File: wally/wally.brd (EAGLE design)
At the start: 41 x 101 mm, 102 parts, among them IC1 ESP32-S3-WROOM-1U-N16, IC2 XTLV61048DBVR, IC3 TLV1117LV33DCYR, IC4 DPS310XTSA1, IC6 LSM6DSV16BXTR, IC7 MLX90395KLW-BBA-001-SP, J1 MSD-4-A, J2 QWIIC_RIGHT_ANGLE, J3 QWIIC_RIGHT_ANGLE, J5 USB4105-GF-A, U1 RA-01H

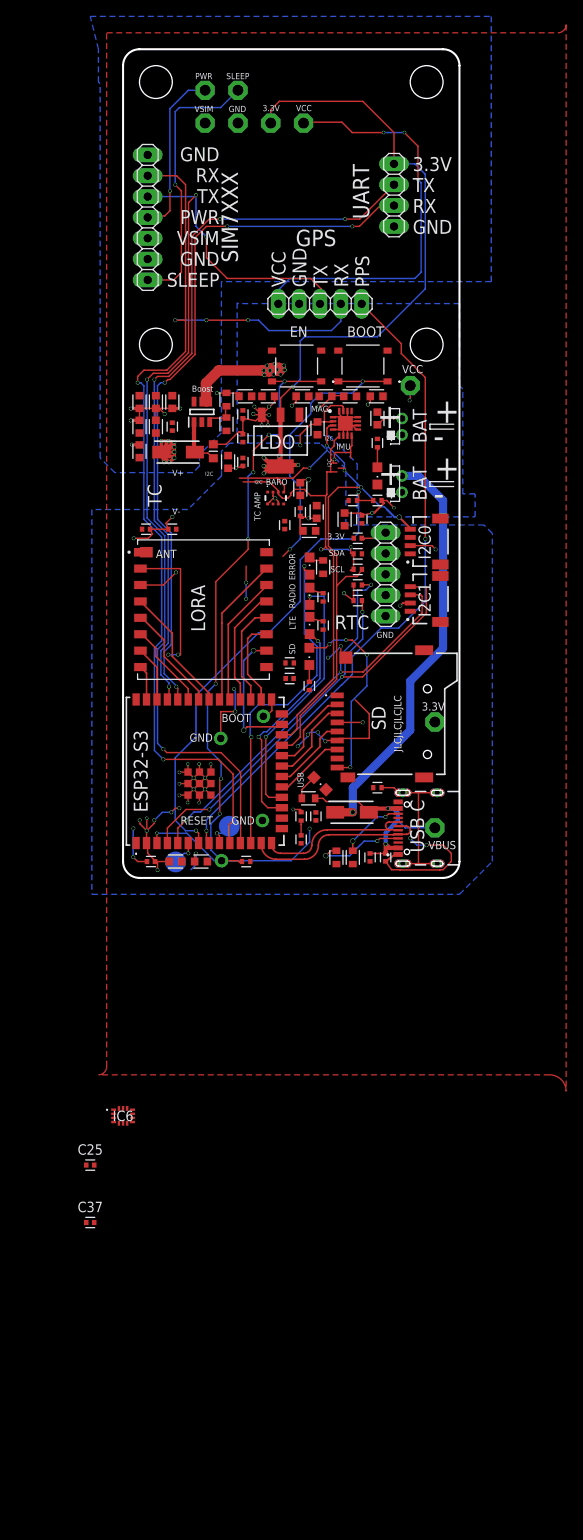
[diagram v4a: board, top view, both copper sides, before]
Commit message: rewire qwiic connectors
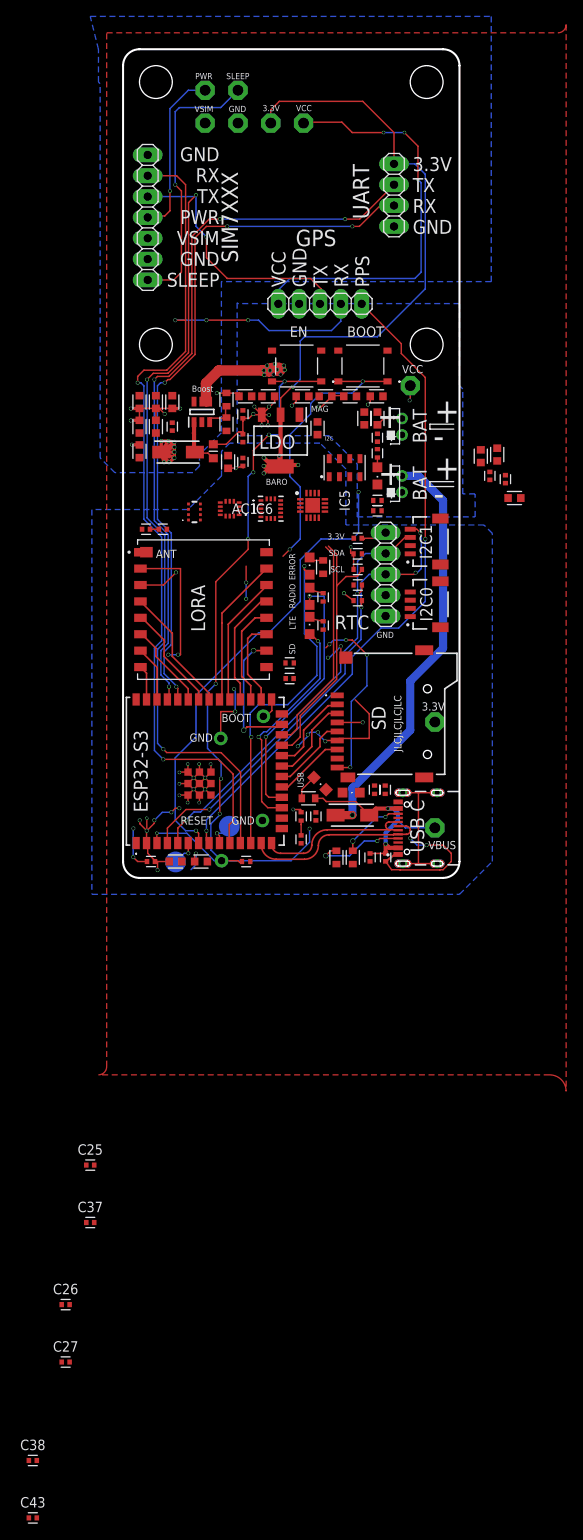
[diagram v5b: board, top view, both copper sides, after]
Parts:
- added AC1: H3LIS331DLTR, SamacSys_Parts:LIS3DHTR
- added C26, C27, C38, C43: 100n, Capacitor:CAPC1005X60
- added IC5: MS560702BA03-50, SamacSys_Parts:MS5607-02BA03
- moved IC6 75.1 mm to (13.0, -56.0), turned to 180 degrees
- moved C28 25.7 mm to (44.7, -52.0)
- moved C42 25.3 mm to (47.7, -54.7)
- moved C29 25.3 mm to (46.6, -52.4)
- moved C41 23.1 mm to (45.6, -49.4)
- moved C40 22.4 mm to (43.6, -49.6)
- moved LED1 17.4 mm to (27.8, -90.6), turned to 270 degrees
- moved R15 14.9 mm to (30.6, -90.2), turned to 90 degrees
- moved C7 12.5 mm to (29.4, -45.0), turned to 270 degrees
- moved IC7 10.8 mm to (23.1, -55.6)
- moved C1 10.1 mm to (31.0, -47.4), turned to 90 degrees
- moved IC4 10.0 mm to (8.70, -56.4), turned to 270 degrees
- moved J2 7.65 mm to (35.0, -67.7)
- moved J3 7.00 mm to (35.0, -60.0)
- moved R10 3.25 mm to (31.0, -56.2), turned to 0 degrees
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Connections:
- removed net N$5: IC6.14
- removed net N$6: IC6.13
- net 3V3: now also AC1.1, AC1.14, AC1.15, AC1.8, C26.1, C27.1, C38.1, C43.1, IC5.1, IC5.2
- net GND: now also AC1.10, AC1.12, AC1.13, AC1.16, AC1.5, AC1.7, C26.2, C27.2, C38.2, C43.2, IC5.3, IC5.4, IC5.5, IC5.6
- net SCL0: now also AC1.4, IC5.8, IC6.13
- net SDA0: now also AC1.6, IC5.7, IC6.14
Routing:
- net SCL0: track 76.5 -> 32.5 mm, vias 5 -> 0
- net 3V3: track 165.4 -> 127.4 mm, vias 29 -> 20
- net SDA0: track 58.6 -> 26.6 mm, vias 1 -> 0
- net GND: track 108.9 -> 95.3 mm
- net VCC: track 162.1 -> 153.2 mm, vias 26 -> 24
- net SDA1: track 59.9 -> 53.3 mm, vias 3 -> 2
- net VSENSE: track 60.1 -> 56.9 mm
- net SHLD: track 19.8 -> 17.5 mm
- net N$1: track 2.04 -> 0.00 mm
- net N$49: track 24.3 -> 22.3 mm
- net SCL1: track 59.8 -> 58.2 mm, vias 3 -> 4
- net N$9: track 2.49 -> 1.19 mm
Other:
- board text removed: "IMU"
- board text removed: "TC AMP"

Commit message: route new i2c traces
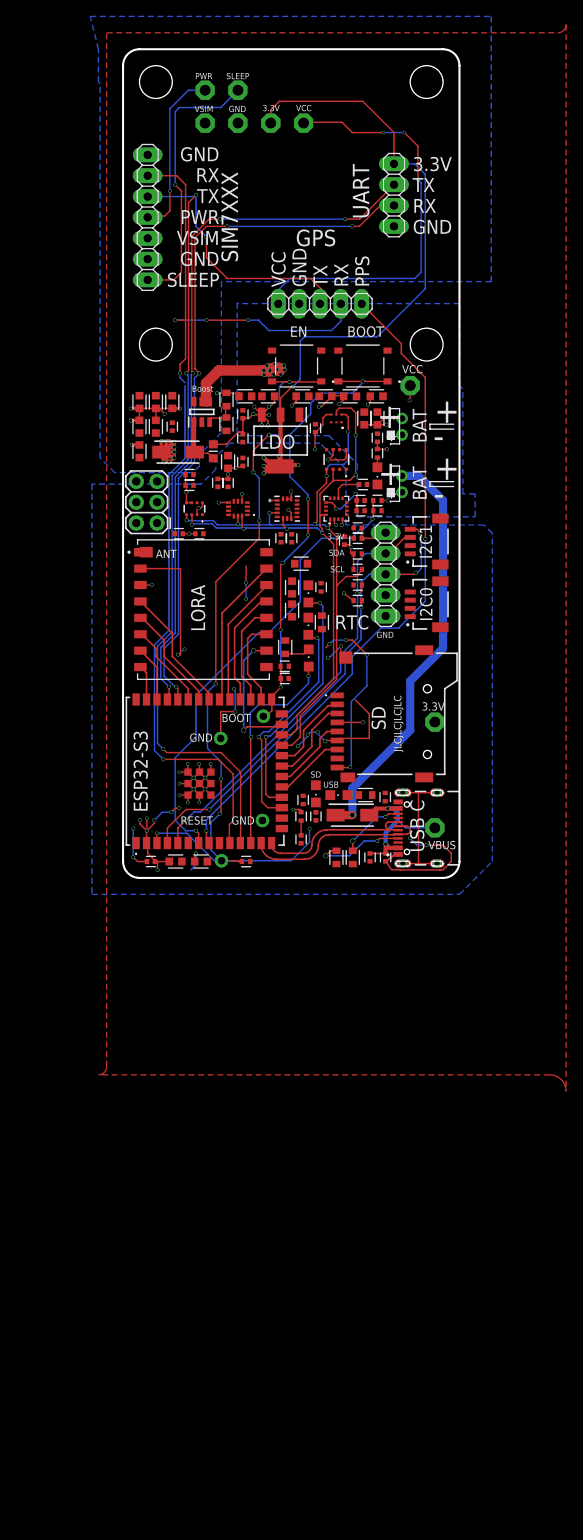
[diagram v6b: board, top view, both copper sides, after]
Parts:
- removed IC5: MS560702BA03-50, SamacSys_Parts:MS5607-02BA03
- removed TP14, TP15: PTR1B2,54, testpad:B2,54
- added C44, C46: 1u, Capacitor:CAPC1005X60
- added C45: 100n, Capacitor:CAPC1005X60
- added IC8: APDS-9253-001, SamacSys_Parts:APDS9253001
- added IC9: BME688, SamacSys_Parts:BME688
- added J6: FEMALE 2x3, SparkFun-Connectors:2X3
- C24: value 470n -> 10u; device Capacitor:CAPC1608X85 -> Capacitor:CAPC1005X60
- IC4: value DPS310XTSA1 -> DPS368XTSA1; device SamacSys_Parts:DPS310XTSA1 -> SamacSys_Parts:DPS368XTSA1
- IC7: value MLX90395KLW-BBA-001-SP -> MMC5983MA; device SamacSys_Parts:QFN50P300X300X100-17N -> SamacSys_Parts:MMC5983MA
- LED5: value LEDG -> LEDY
- R19: value 33 -> 75; device Resistor:RESC1005X40 -> Resistor:RESC1608X60
- R5, R6, R7, R8: value 10k -> 5k1
- moved C43 129.1 mm to (28.9, -56.2)
- moved C38 123.6 mm to (28.9, -55.0)
- moved C27 104.1 mm to (20.6, -59.6), turned to 270 degrees
- moved C26 97.0 mm to (19.2, -59.6), turned to 270 degrees
- moved C37 91.7 mm to (12.8, -52.9), turned to 270 degrees
- moved C25 84.6 mm to (11.6, -52.9), turned to 270 degrees
- moved C29 38.5 mm to (8.10, -53.1), turned to 0 degrees
- moved C28 36.6 mm to (8.10, -51.9), turned to 0 degrees
- moved C41 31.4 mm to (20.6, -68.4)
- moved C40 28.0 mm to (20.6, -65.6)
- moved C42 27.2 mm to (21.7, -62.7)
- moved LED6 11.2 mm to (22.6, -74.2)
- moved R20 10.8 mm to (19.8, -72.9), turned to 90 degrees
- moved C24 8.82 mm to (29.2, -53.0), turned to 0 degrees
- moved R15 8.79 mm to (21.9, -91.5)
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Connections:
- removed net ERR_LED: IC1.12, LED6.A
- removed net LTE_STATUS: IC1.17, LED4.A
- removed net RAD_STATUS: IC1.18, LED5.A
- new net A2: IC1.18, J6.6, LED4.A
- new net A3: IC1.6, J6.3
- new net A4: IC1.9, J6.5
- new net N$6: C24.1, IC7.10
- net 3V3: now also C44.1, C45.1, C46.1, IC4.5, IC7.13, IC7.4, IC8.4, IC9.2, IC9.6, IC9.8; no longer C24.2, IC5.1, IC5.2, IC7.15, IC7.8
- net A0: now also IC1.12, J6.2, LED6.A; no longer IC1.6, TP15.TP
- net A1: now also IC1.17, J6.4, LED5.A; no longer IC1.9, TP14.TP
- net GND: now also C24.2, C44.2, C45.2, C46.2, IC8.1, IC9.1, IC9.5, IC9.7, J6.1; no longer C24.1, IC5.3, IC5.4, IC5.5, IC5.6, IC7.1, IC7.10, IC7.12, IC7.13, IC7.14, IC7.16, IC7.17, IC7.4, IC7.6, IC7.7
- net SCL0: now also IC7.1, IC8.6, IC9.4; no longer IC5.8, IC7.3
- net SDA0: now also IC7.16, IC8.5, IC9.3; no longer IC5.7, IC7.5
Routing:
- net SDA0: track 26.6 -> 72.6 mm, vias 0 -> 6
- net SCL0: track 32.5 -> 75.0 mm, vias 0 -> 7
- net ERR_LED: track 41.2 -> 0.00 mm, vias 2 -> 0
- net RAD_STATUS: track 32.0 -> 0.00 mm, vias 2 -> 0
- net 3V3: track 127.4 -> 158.4 mm, vias 20 -> 36
- net A2: track 0.00 -> 30.1 mm, vias 0 -> 2
- net LTE_STATUS: track 27.3 -> 0.00 mm, vias 2 -> 0
- net A1: track 3.18 -> 27.6 mm, vias 1 -> 2
- net A0: track 3.24 -> 26.6 mm, vias 1 -> 2
- net BOOT: track 37.3 -> 58.8 mm, vias 2 -> 6
- net VBUS: track 26.8 -> 19.4 mm
- net VCC: track 153.2 -> 159.9 mm, vias 24 -> 28
- net RX1: track 123.9 -> 119.7 mm
- net N$6: track 0.00 -> 3.90 mm
- net N$4: track 3.15 -> 0.00 mm
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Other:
- board text removed: "BARO"
- board text removed: "ERROR"
- board text removed: "I2C"
- board text removed: "LTE"
- board text removed: "MAG"
- board text removed: "RADIO"

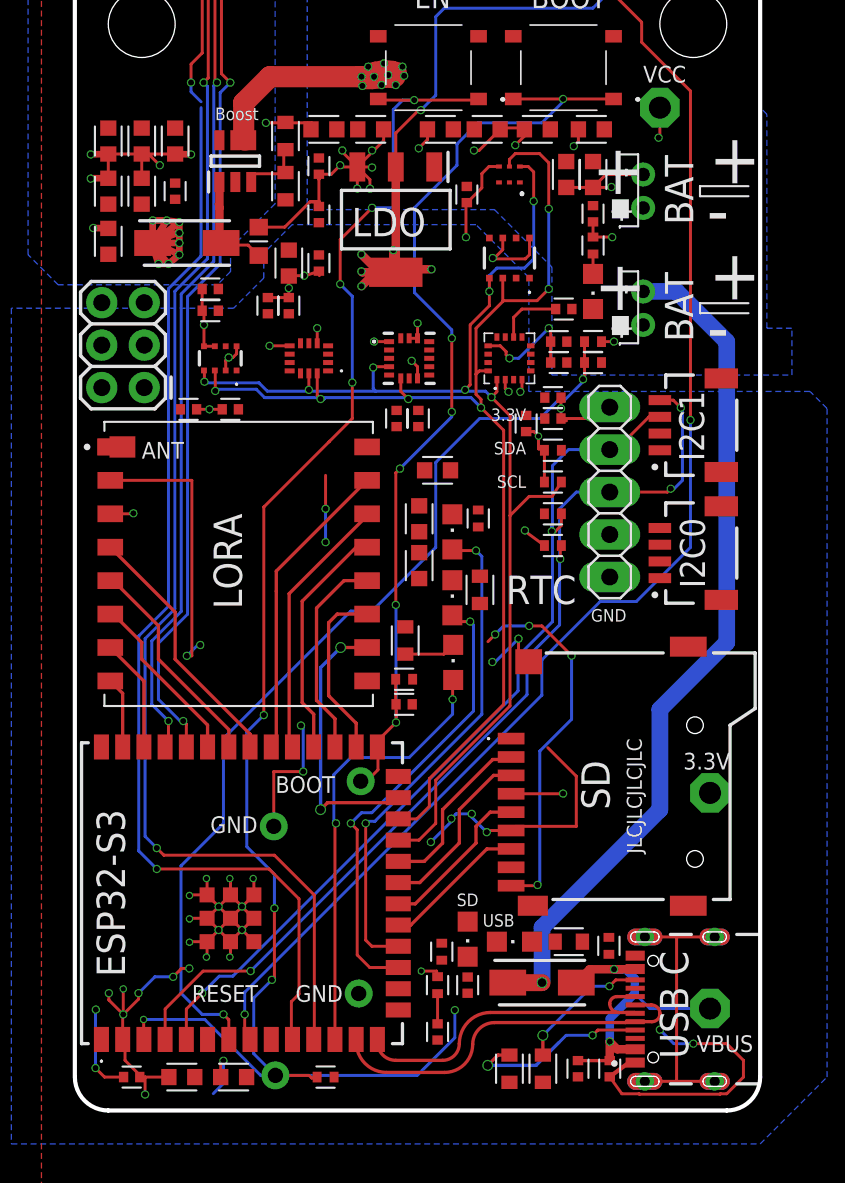
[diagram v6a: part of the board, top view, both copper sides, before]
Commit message: complete routing
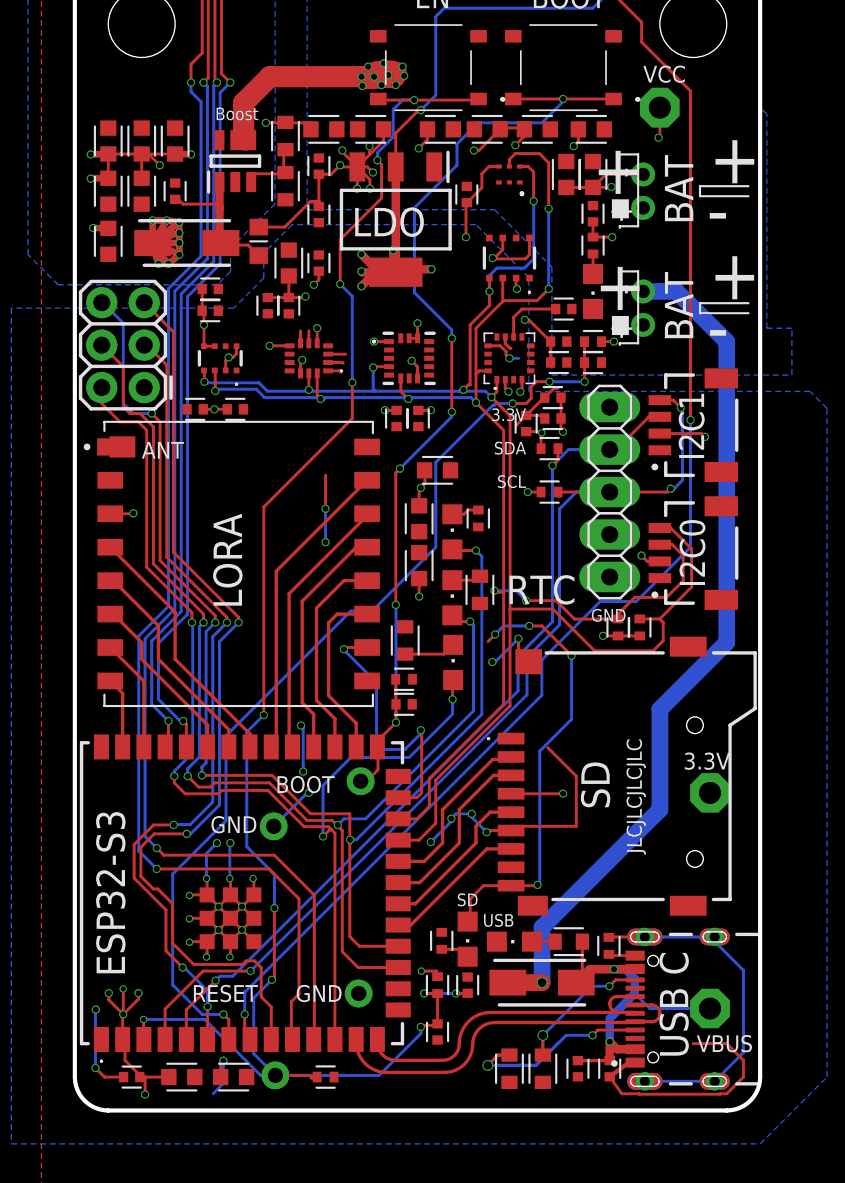
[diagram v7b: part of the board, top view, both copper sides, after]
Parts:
- moved R5 11.3 mm to (32.5, -72.1), turned to 90 degrees
- moved R6 10.1 mm to (33.8, -72.1), turned to 90 degrees
- moved R7 3.91 mm to (28.4, -61.4)
- moved R8 3.21 mm to (28.4, -64.0)
- moved R15 0.65 mm to (21.9, -90.8)
- moved C23 0.40 mm to (7.20, -59.0)
- moved C19 0.30 mm to (9.60, -59.0)
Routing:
- net A4: track 0.00 -> 55.9 mm, vias 0 -> 2
- net A3: track 0.00 -> 49.1 mm, vias 0 -> 4
- net A2: track 30.1 -> 75.0 mm, vias 2 -> 5
- net A1: track 27.6 -> 68.7 mm, vias 2 -> 4
- net A0: track 26.6 -> 65.8 mm, vias 2 -> 4
- net SCL0: track 75.0 -> 91.8 mm
- net SDA0: track 72.6 -> 89.1 mm, vias 6 -> 8
- net GND: track 95.0 -> 89.7 mm, vias 28 -> 27
- net N$49: track 22.3 -> 26.5 mm
- net SHLD: track 17.5 -> 21.2 mm
- net VBUS: track 19.4 -> 22.0 mm
- net N$2: track 6.89 -> 9.44 mm
- net SCL1: track 58.2 -> 60.5 mm, vias 4 -> 3
- net 3V3: track 158.4 -> 160.5 mm, vias 36 -> 43
- net N$8: track 0.51 -> 2.26 mm
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
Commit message: export new wally
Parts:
- J6: device SparkFun-Connectors:2X3 -> SparkFun-Connectors:2X3-NS
- moved J6 2.91 mm to (2.85, -55.1)
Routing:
- net GND: track 89.7 -> 115.9 mm, vias 27 -> 40
- net N$49: track 26.5 -> 4.19 mm, vias 4 -> 0
- net 3V3: track 160.5 -> 181.1 mm, vias 43 -> 45
- net A3: track 49.1 -> 49.7 mm
- net N$8: track 2.26 -> 1.75 mm
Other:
- board text added: "A2"
- board text added: "A3"
- board text added: "A4"
- board text added: "ACC"
- board text added: "ALS"
- board text added: "ART Avionics"
- board text added: "Akshat Tripathi"
- board text added: "BARO"
- board text added: "Designed by Shrey Bohra"
- board text added: "ENV"
- board text added: "Ella Devsea"
- board text added: "Hritik Parmessur"
- board text added: "I2C"
- board text added: "IMU"
- board text added: "MAG"
- board text removed: "Designed by ART Avionics"
- board text removed: "TC"
- board text removed: "V+"
- board text removed: "V-"
